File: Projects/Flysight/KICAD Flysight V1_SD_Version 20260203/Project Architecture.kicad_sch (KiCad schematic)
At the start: 0 parts

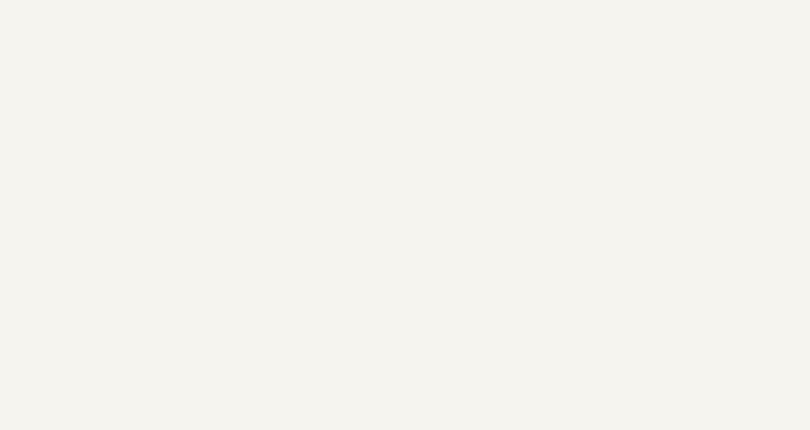
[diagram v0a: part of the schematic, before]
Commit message: Commit 2: PaginaMock Added
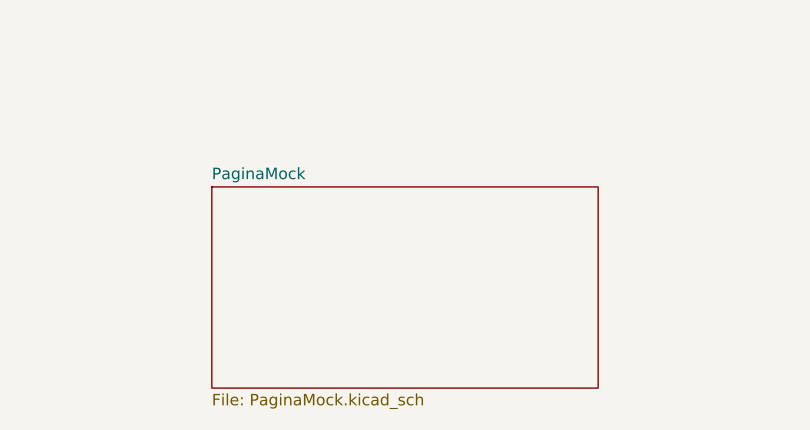
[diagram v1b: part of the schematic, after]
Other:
- added sheet PaginaMock (PaginaMock.kicad_sch)
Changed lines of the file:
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@@
+	)
+	(sheet
+		(at 140.716 303.784)
+		(size 42.926 22.352)
+		(exclude_from_sim no)
+		(in_bom yes)
+		(on_board yes)
+		(dnp no)
+		(fields_autoplaced yes)
+		(stroke
+			(width 0.1524)
+			(type solid)
+		)
+		(fill
+			(color 0 0 0 0.0000)
+		)
+		(property "Sheetname" "PaginaMock"
+			(at 140.716 303.0724 0)
+			(effects
+				(font
+					(size 1.27 1.27)
+				)
+				(justify left bottom)
+			)
+		)
+		(property "Sheetfile" "PaginaMock.kicad_sch"
+			(at 140.716 326.7206 0)
+			(effects
+				(font
+					(size 1.27 1.27)
+				)
+				(justify left top)
+			)
+		)
+		(instances
+			(project "Flysight V1_SD_Version"
+				(path "/0650c7a8-acba-429c-9f8e-eec0baf0bc1c/fede4c36-00cc-4d3d-b71c-5243ba232202"
+					(page "25")
+				)
+			)
+		)
 	)
 	(sheet
